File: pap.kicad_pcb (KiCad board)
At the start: 2 copper layers, 60 x 60 mm, 47 parts, among them J1 Conn_01x02, J3 Conn_01x04, J6 Conn_01x02, U1 powerstep01

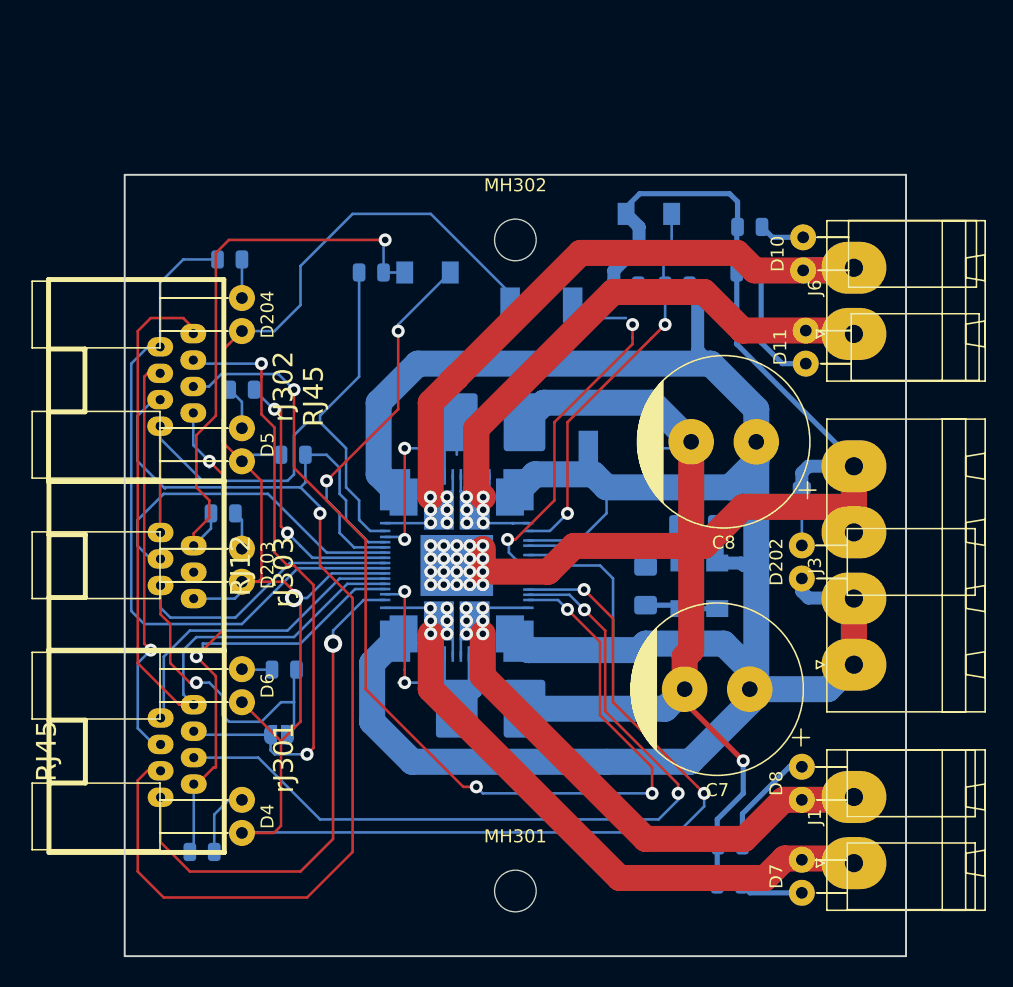
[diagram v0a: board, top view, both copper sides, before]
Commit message: sigo ruteando, serigrafia mas gruesa, alineacino etc
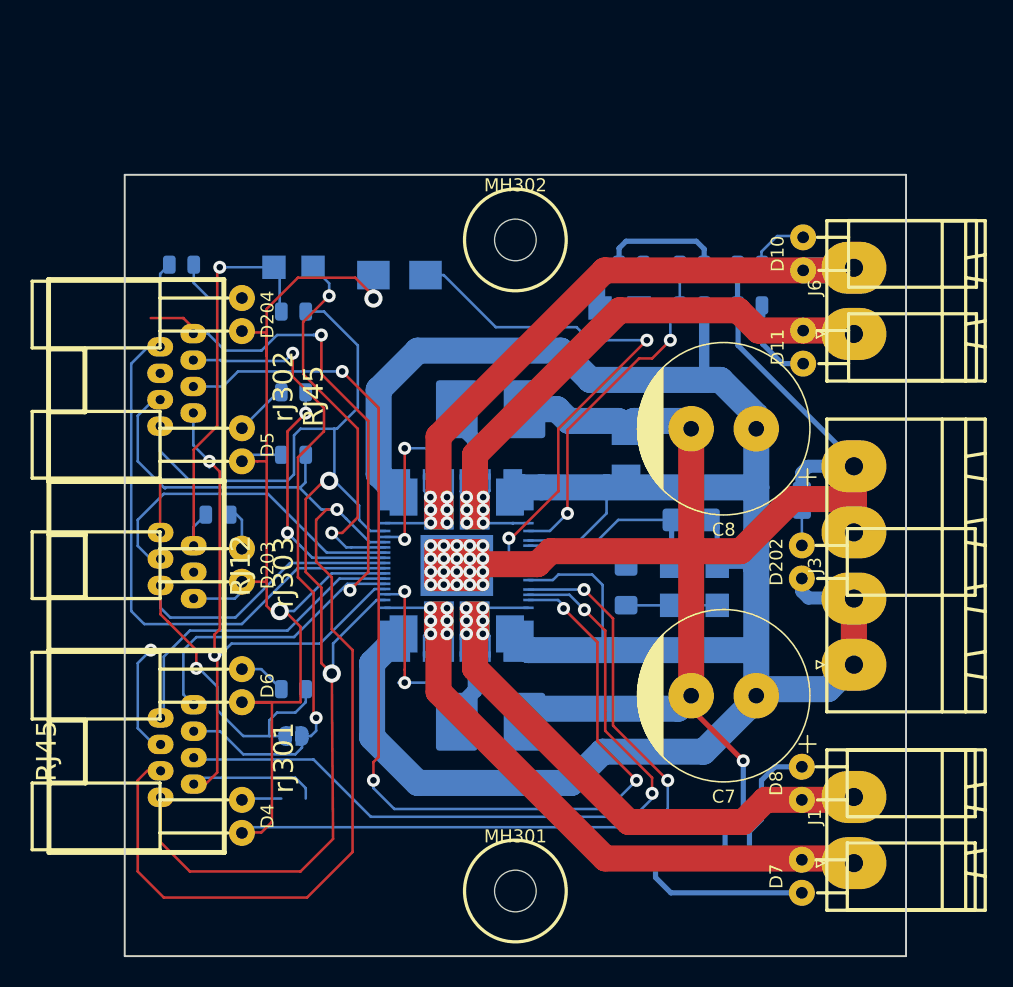
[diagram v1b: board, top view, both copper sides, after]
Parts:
- removed R8: R, Resistor_SMD:R_0805_2012Metric
- C1, C6: footprint Capacitor_SMD:C_0805_2012Metric -> pap:C_0805_2012Metric
- C4, C5: footprint Capacitor_SMD:C_1206_3216Metric_Pad1.42x1.75mm_HandSolder -> pap:C_1206_3216Metric_Pad1.42x1.75mm_HandSolder
- D1, D9: footprint Diode_SMD:D_MELF -> pap:D_SMA
- D12, D2, D201, D3: footprint Diode_SMD:D_MiniMELF -> pap:D_MiniMELF
- JP1: footprint Jumper:SolderJumper-2_P1.3mm_Open_RoundedPad1.0x1.5mm -> pap:SolderJumper-2_P1.3mm_Open_RoundedPad1.0x1.5mm
- MH301, MH302: footprint MountingHole:MountingHole_3.2mm_M3 -> pap:MountingHole_3.2mm_M3
- R10, R11, R12, R13, R14, R201, R202, R203, R204, R6, R7, R9: footprint Resistor_SMD:R_0805_2012Metric -> pap:R_0805_2012Metric
- R3, R4: footprint Resistor_SMD:R_2816_7142Metric_Pad3.20x4.45mm_HandSolder -> pap:R_2816_7142Metric_Pad3.20x4.45mm_HandSolder
- moved D9 11.1 mm to (113.6, 90.2)
- moved D201 10.3 mm to (105.5, 89.6)
- moved D12 7.57 mm to (130.5, 92.7)
- moved C1 6.69 mm to (105.5, 93.0), turned to 180 degrees
- moved R7 5.31 mm to (136.1, 89.4), turned to 0 degrees
- moved R11 5.07 mm to (134.2, 135.2), turned to 180 degrees
- moved R9 3.97 mm to (105.5, 99.2)
- moved R204 3.72 mm to (96.9, 89.4)
- moved R13 2.90 mm to (140.5, 89.4)
- moved R14 2.53 mm to (140.5, 92.5)
- moved R6 1.90 mm to (136.1, 92.5)
- moved C6 1.78 mm to (131.4, 89.4)
- moved R10 1.66 mm to (105.5, 122.0)
- moved C5 1.50 mm to (131.0, 114.1)
- moved R12 1.31 mm to (139.5, 135.2)
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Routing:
- net /connector/Sdo_Back: track 31.2 -> 8.68 mm
- net G3V3: track 89.9 -> 106.4 mm, vias 1 -> 2
- net 3v3: track 159.6 -> 145.6 mm, vias 3 -> 4
- net 15v: track 31.6 -> 45.3 mm
- net G85V: track 161.2 -> 174.6 mm
- net /connector/Switch: track 44.6 -> 32.6 mm
- net Net-(D7-Pad1): track 4.89 -> 13.0 mm
- net 85v: track 206.0 -> 198.1 mm
- net /connector/MotorB1: track 52.3 -> 59.2 mm
- net /connector/Osc_Out: track 79.3 -> 85.8 mm
- net /connector/MotorB2: track 57.5 -> 63.5 mm
- net /connector/MotorA1: track 51.4 -> 56.7 mm
- net /connector/Busy_Out: track 47.6 -> 51.5 mm
- net /connector/MotorA2: track 57.2 -> 61.0 mm
- net /connector/Reset: track 90.3 -> 86.6 mm
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
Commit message: agregando mascaras para alambrado de pistas tie-net,
agregando mascaras para soldar alambres en pistas de potencia, uno con
tie net gnd de 3 con el gnd de 85, tambien agrego planos de tierra para
ambos, y asuntos relacionados con eso. mejor el 3d de las rj;s, agrego
gerbers del fabricante, recien lo veo!! pero se parece bastante a lo que
hice..
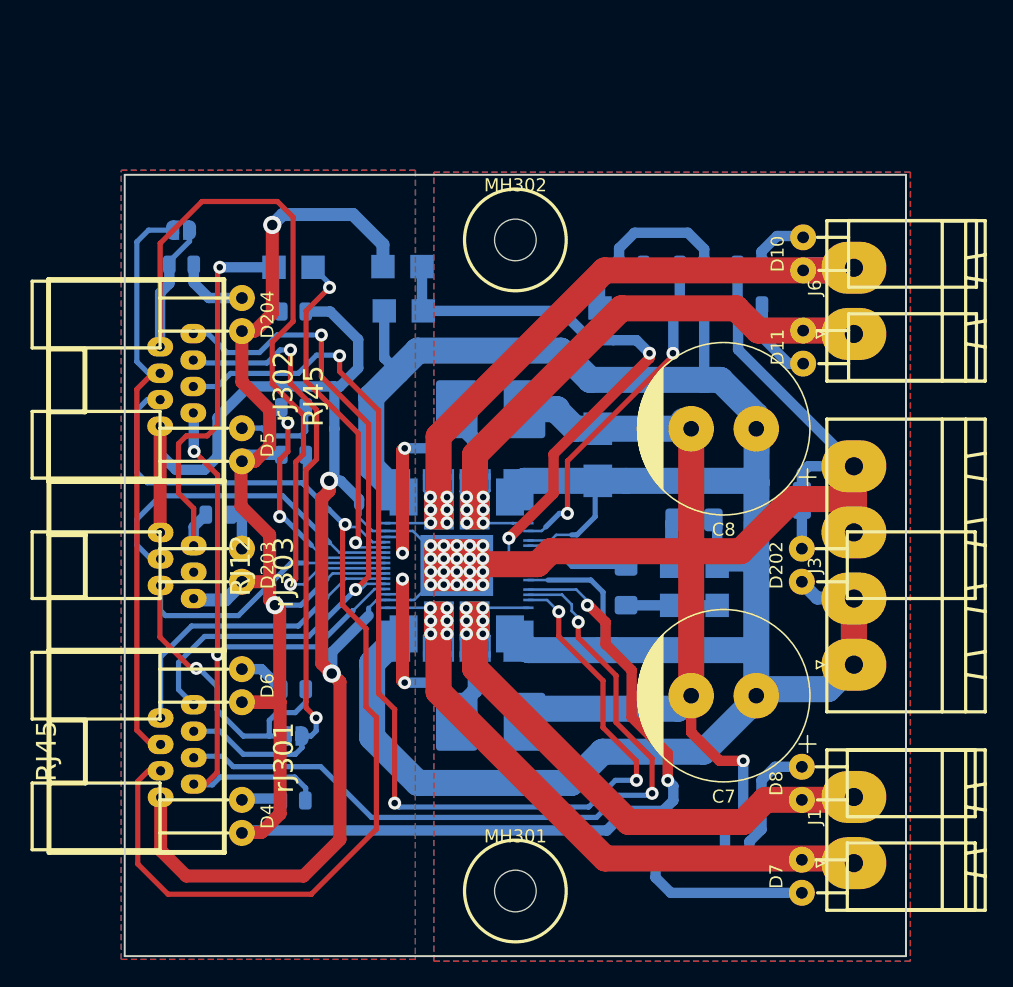
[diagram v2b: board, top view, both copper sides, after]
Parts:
- removed D9: SM4007, pap:D_SMA
- added D205: LL4148, pap:D_MiniMELF, B.Cu at (113.8, 89.5)
- added D206: LL4148, pap:D_MiniMELF, B.Cu at (113.9, 92.9)
- added JP301: jumper, pap:SolderJumper-2_P1.3mm_Open_RoundedPad1.0x1.5mm, B.Cu at (96.8, 86.7)
- added NT301: Net-Tie_2, pap:NetTie-2_SMD_Pad0.2mm_sin_seri, B.Cu at (114.3, 115.1)
- added NT302: Net-Tie_2, pap:NetTie-2_SMD_Pad0.2mm_sin_seri, B.Cu at (114.1, 109.8)
- added R8: R, pap:R_0805_2012Metric, B.Cu at (105.4, 130.5)
- moved D1 2.17 mm to (128.8, 104.0)
- moved R9 1.15 mm to (105.5, 100.3), turned to 0 degrees
- moved D202 0.25 mm to (144.5, 113.7)
- moved C4 0.22 mm to (136.2, 109.0)
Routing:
- net /connector/Sdo_Back: track 8.68 -> 45.8 mm, vias 1 -> 0
- net /connector/SDO: track 50.0 -> 67.9 mm, vias 0 -> 1
- net G85V: track 174.6 -> 185.5 mm
- net G3V3: track 106.4 -> 111.2 mm
- net /connector/CLK: track 59.1 -> 55.0 mm
- net 85v: track 198.1 -> 202.1 mm
- net Net-(D5-Pad1): track 4.17 -> 7.14 mm
- net 3v3: track 145.6 -> 148.1 mm
- net /motor/Switch_Local: track 29.1 -> 26.7 mm
- net 15v: track 45.3 -> 47.7 mm
- net /connector/Switch: track 32.6 -> 34.5 mm
- net /connector/Reset: track 86.6 -> 84.9 mm
- net /motor/SenseB: track 23.5 -> 22.5 mm
- net /connector/CS: track 56.5 -> 55.6 mm
- net /motor/Flag: track 19.7 -> 18.8 mm
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- added copper zone on B.Cu, net G3V3
- added copper zone on F.Cu, net G3V3
- added copper zone on B.Cu, net G85V
- added copper zone on F.Cu, net G85V

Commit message: cambio de nombres, mejorop serigrafia, agrego pin
agrego el pin de flag ya que me sobraba un pin en el RJ12, cambio los
nombres de 0-50 para motor y 51 a 100 para conector, ajusto el espesor
de la seri, y algunas cosas mas..
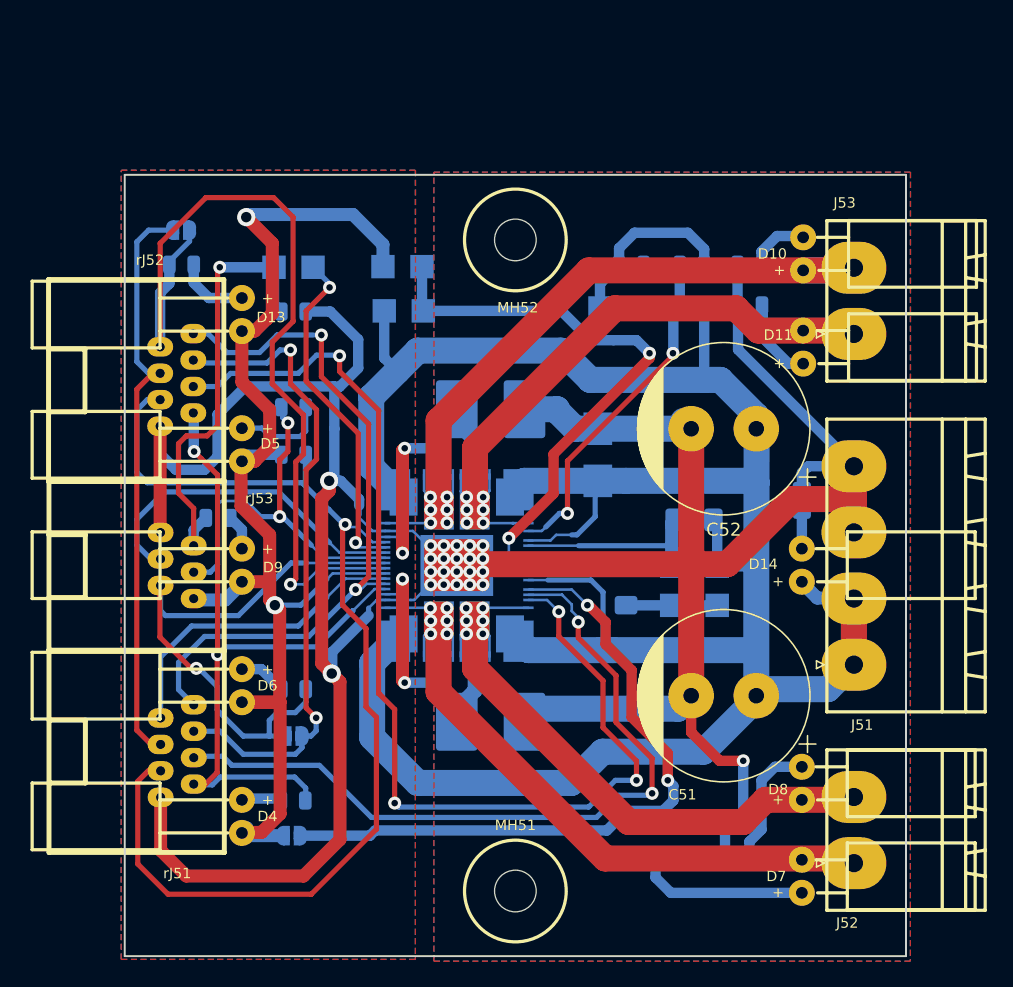
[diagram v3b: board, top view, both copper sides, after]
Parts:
- removed D1: SM4007, pap:D_SMA
- removed D202: LED_I, pap:led5p_enchufable
- added D14: LED_I, pap:led5p_enchufable, F.Cu at (144.5, 113.7)
- added D51: SM4007, pap:D_SMA, B.Cu at (128.8, 104.0)
- added JP2: jumper, pap:SolderJumper-2_P1.3mm_Open_RoundedPad1.0x1.5mm, B.Cu at (105.3, 133.2)
- moved R203 0.25 mm to (99.7, 108.8)
- renumbered C7 to C51, C8 to C52, D204 to D13, D205 to D15, D206 to D16, D201 to D17, D203 to D9, J3 to J51, J1 to J52, J6 to J53, JP1 to JP51, JP301 to JP52, MH301 to MH51, MH302 to MH52, NT301 to NT51, NT302 to NT52, R201 to R1, rJ301 to rJ51, rJ302 to rJ52, rJ303 to rJ53
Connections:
- D13 pad 2: 3v3 -> 3V3
- D15 pad 2: 3v3 -> 3V3
- D4 pad 2: 3v3 -> 3V3
- D5 pad 2: 3v3 -> 3V3
- D6 pad 2: 3v3 -> 3V3
- D9 pad 2: 3v3 -> 3V3
- R1 pad 2: 3v3 -> 3V3
- R9 pad 1: /motor/Flag -> /connector/Flag
- U1 pad 13: 3v3 -> 3V3
- U1 pad 16: /motor/Flag -> /connector/Flag
- U1 pad 62: 3v3 -> Vreg
- rJ53 pad 1: 3v3 -> 3V3
- rJ53 pad 3: Net-(rJ303-Pad3) -> /connector/Flag
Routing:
- net 3v3: track 148.1 -> 0.00 mm, vias 4 -> 0
- net 3V3: track 0.00 -> 98.2 mm, vias 0 -> 2
- net Vreg: track 0.00 -> 52.3 mm, vias 0 -> 2
- net /connector/Flag: track 0.00 -> 30.8 mm, vias 0 -> 2
- net /motor/Flag: track 18.8 -> 0.00 mm, vias 2 -> 0
- net /connector/MotorA2: track 61.0 -> 61.7 mm

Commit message: aghrego serigrafia, logos, faltan fiduciales aun
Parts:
- added L101: logo_dci, pap:logo_neurona_15mm, F.Cu at (116.6, 133.1)
- added L102: logo_kicad, Symbol:KiCad-Logo2_6mm_SilkScreen, B.Cu at (135.7, 138.2)
- added L104: logo_cnc, pap:cnc, F.Cu at (113.0, 89.2)
- added L401: logo_recyclado, Symbol:WEEE-Logo_4.2x6mm_SilkScreen, B.Cu at (96.1, 137.8)
- added LOGO103: Logo_Open_Hardware_Small, Symbol:OSHW-Logo2_14.6x12mm_SilkScreen, B.Cu at (112.0, 135.8)
- renumbered rJ51 to J54, rJ52 to J55, rJ53 to J56, MH51 to MH101, MH52 to MH102
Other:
- board text added: "0v Vin"
- board text added: "3875"
- board text added: "3v3 Sel"
- board text added: "Bariloche Argentina"
- board text added: "Bsy Sel"
- board text added: "CLK SDI BSY SDO OSC_OUT RST CS GND"
- board text added: "CLK SDI BSY SDO_B OSC_IN RST CS GND"
- board text added: "GND SW PUL FLG BSY 3V3"
- board text added: "MA1"
- board text added: "MA2"
- board text added: "MB1"
- board text added: "MB2"
- board text added: "PS20181310"
- board text added: "PaP"
- board text added: "SDO Sel"
- board text added: "disenioconingenio"

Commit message: voy terminando, me falta sacar los gerbers.. a por ellos...
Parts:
- added F1: Fiducial, pap:Fiducial_1mm_Dia_2mm_Outer, B.Cu at (148.8, 125.3)
- added F2: Fiducial, pap:Fiducial_1mm_Dia_2mm_Outer, B.Cu at (97.0, 133.6)
- added F3: Fiducial, pap:Fiducial_1mm_Dia_2mm_Outer, B.Cu at (114.4, 100.8)
- moved L102 0.50 mm to (135.7, 138.7)
- moved LOGO103 0.40 mm to (112.4, 135.8)
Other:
- board text added: "Bsy"
- board text added: "CS"
- board text added: "Flag"
- board text added: "MA"
- board text added: "MB"
- board text added: "P"
- board text added: "Paste Mask Top ------------------------- Silkscreen Top ------------------------- Solder Mask Top ------------------------- TOP 2Oz ------------------------- FR4 1.6mm ------------------------- Bottom 2 Oz ------------------------- Solder Mask Bottom ------------------------- Silkscreen Bottom ------------------------- Paste Mask Bottom -------------------------"
- board text added: "Pwr"
- board text added: "Rev1.0 #_ _ _ _"
- board text added: "Sdo"
- board text added: "Sw"
- board text added: "a"
- board text removed: "PaP"

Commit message: agrego gerbers.. va quedando peeero falta crc de layout
ahi lo voy liquidando, me convence, pero me falta tirar el crc en layout
que tiene muchos errores principalmente por el tema de que para una
misma net tengo varias restriccinoes solapadas.. vere como hago con eso
y lo cierro.. ser maniana.. me estoy durmiendo..
ha, cambio tambien un poco la jerarquia de dirs asi queda mas ordenadito
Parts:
- L102: footprint Symbol:KiCad-Logo2_6mm_SilkScreen -> pap:KiCad-Logo2_6mm_SilkScreen
- L401: footprint Symbol:WEEE-Logo_4.2x6mm_SilkScreen -> pap:WEEE-Logo_4.2x6mm_SilkScreen
- LOGO103: footprint Symbol:OSHW-Logo2_14.6x12mm_SilkScreen -> pap:OSHW-Logo2_14.6x12mm_SilkScreen

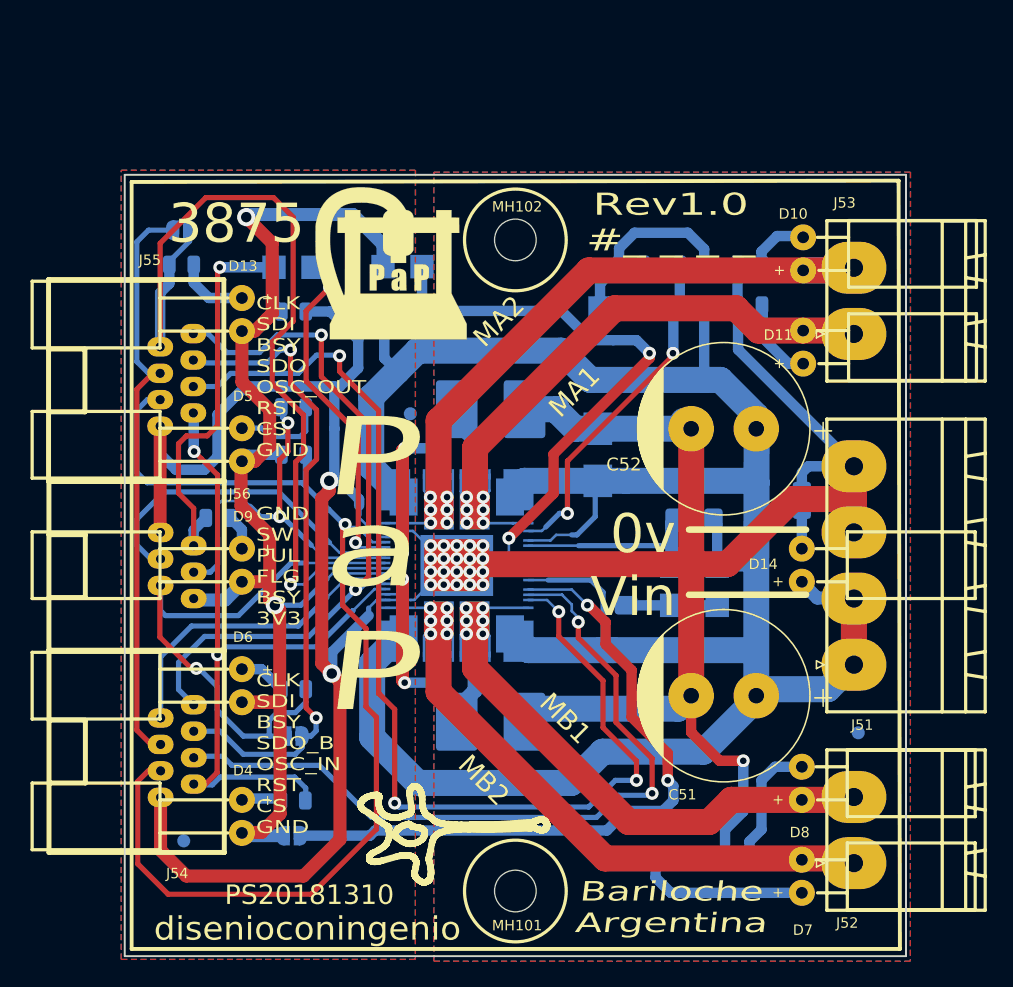
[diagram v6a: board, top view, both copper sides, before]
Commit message: me habia olvidado algunos capas, agrego leds, me falta aun
no estaba poniendo los descaoples de los reguladores internos y hay uno
de 220uF! ese lo mando TH, igual voy a verificar en el PCB de st. pero
igual me faltaban tambien los capas de 3v3 y 85v tambien.. veo donde los
meto
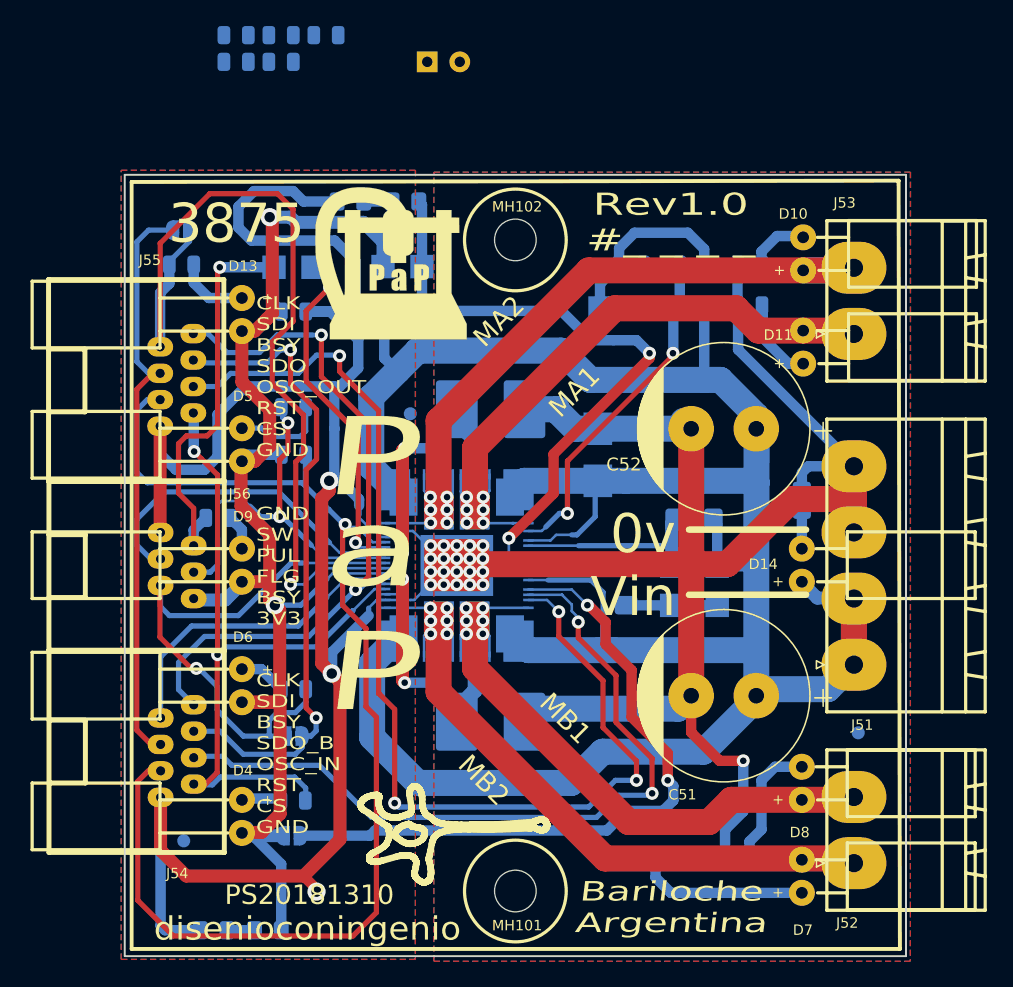
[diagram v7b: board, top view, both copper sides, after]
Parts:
- added C2: C, pap:C_0805_2012Metric, B.Cu at (108.0, 71.8)
- added C3: 220uFx25v, Capacitor_THT:CP_Radial_D6.3mm_P2.50mm, B.Cu at (115.7, 73.8)
- added C7: C, pap:C_0805_2012Metric, B.Cu at (104.5, 71.8)
- added C8: C, pap:C_0805_2012Metric, B.Cu at (104.5, 73.8)
- added C9: C, pap:C_0805_2012Metric, B.Cu at (101.1, 71.8)
- added D1: LED_SMD, pap:Wo_Paste_LED_0805_2012Metric_Pad1.15x1.40mm_HandSolder, B.Cu at (114.1, 84.5)
- added D18: LED_SMD, pap:Wo_Paste_LED_0805_2012Metric_Pad1.15x1.40mm_HandSolder, B.Cu at (103.5, 140.5)
- added R15: R, pap:R_0805_2012Metric, B.Cu at (101.1, 73.8)
- added R2: R, pap:Wo_Paste_R_0805_2012Metric_Pad1.15x1.40mm_HandSolder, B.Cu at (109.8, 84.5)
- added R5: R, pap:Wo_Paste_R_0805_2012Metric_Pad1.15x1.40mm_HandSolder, B.Cu at (99.3, 140.5)
- moved L401 1.03 mm to (95.2, 138.3)
- moved LOGO103 0.41 mm to (112.8, 135.9)
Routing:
- net G3V3: track 111.3 -> 153.2 mm, vias 2 -> 3
- net /connector/Reset: track 84.9 -> 93.0 mm
- net 3V3: track 98.2 -> 104.7 mm
- net 15v: track 47.7 -> 52.8 mm
- net Net-(D1-Pad2): track 0.00 -> 2.26 mm
- net Net-(D18-Pad2): track 0.00 -> 2.20 mm
- net /connector/SDO: track 68.2 -> 68.8 mm
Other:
- board text added: "P&P margin"
- board text added: "SDO"
- board text removed: "SDO Sel"
